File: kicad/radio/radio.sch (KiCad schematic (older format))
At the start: 52 parts, among them J1 SDA, J2 SCL, J3 +5v, J4 +5v, J5 GND1/+12v, J5 GND2, J6 Audio Out, J6 GND2, J7 Antennas, Q1 2N7000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

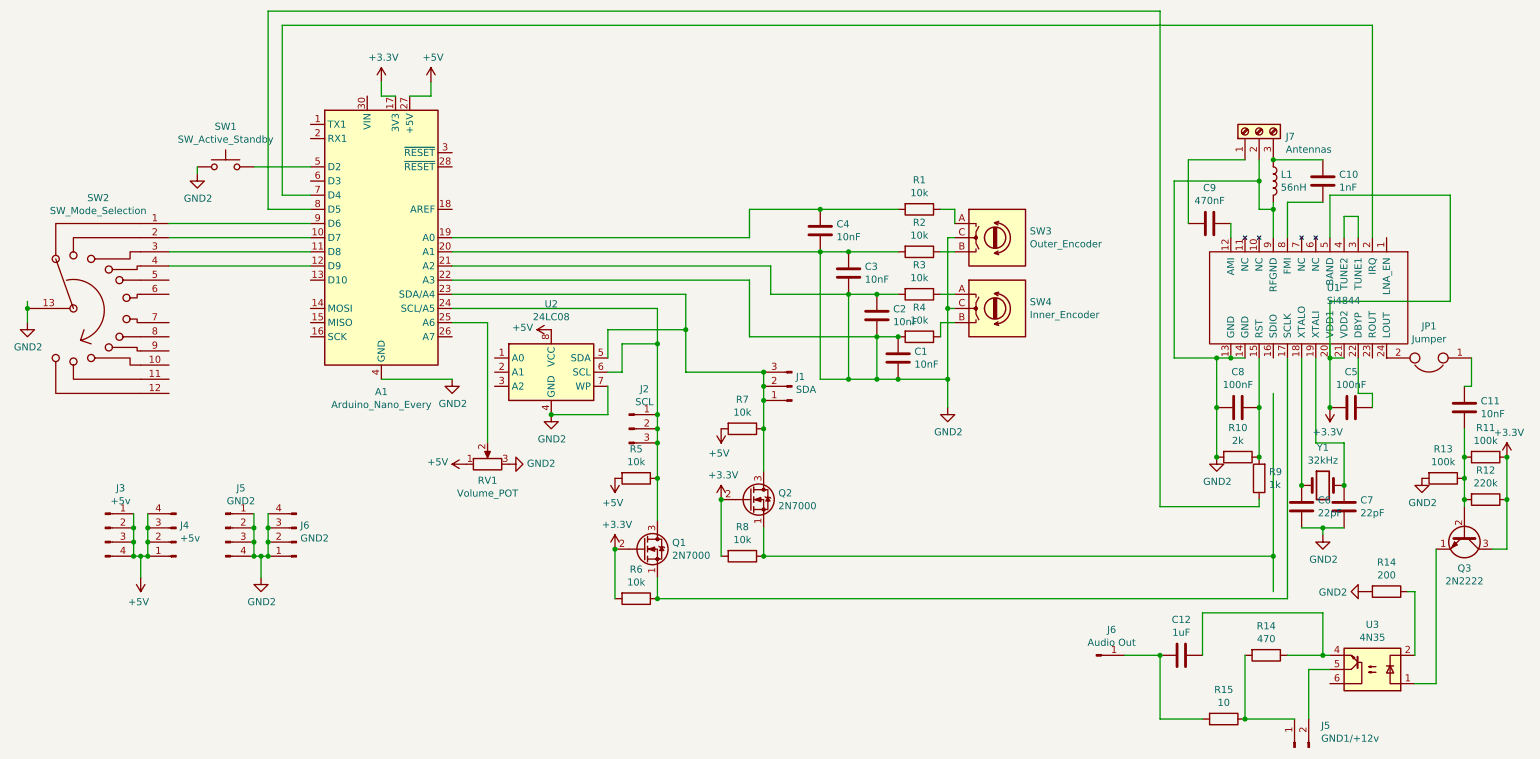
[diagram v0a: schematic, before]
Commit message: improved radio and amplifier schematic
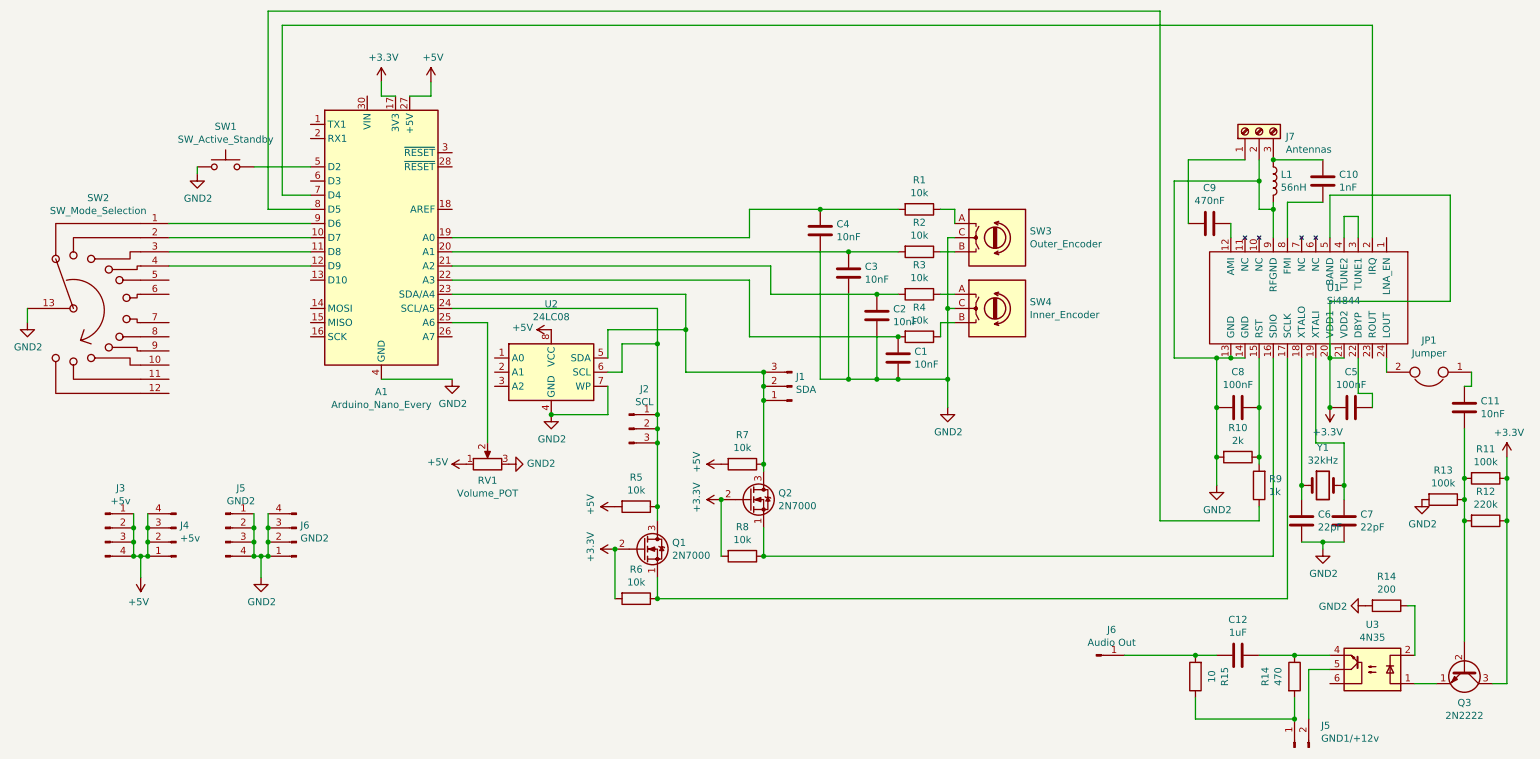
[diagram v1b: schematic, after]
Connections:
- net GND2: no longer A1.20 (A1), A1.21 (A2), A1.22 (A3), C1.2, C2.2, C3.2, R2.2, R3.2, R4.2
- net at U1.16 (SDIO): now also Q2.1 (S), R8.1
- new net: A1.20 (A1), C3.2, R2.2
- new net: A1.21 (A2), C2.2, R3.2
- new net: A1.22 (A3), C1.2, R4.2
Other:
- moved on the sheet: C12, C6, C7, JP1, Q3, R11, R12, R13, R14, R15, R5, R7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

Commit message: Power supply modifications
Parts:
- added C13: 100uF, symbol Device:CP
- added J6: GND2/+5v, symbol Connector:Conn_01x02_Male
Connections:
- net +5V: now also C13.1, J6.2 (Pin_2)
- net GND2: now also C13.2, J6.1 (Pin_1)

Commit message: Only activate squelch after AM transmission is picked up
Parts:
- renumbered J6 to J10, J6 to J8, J5 to J9, R14 to R16
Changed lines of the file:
@@
 Connection ~ 1400 4750
 $Comp
-L Connector:Conn_01x04_Male J5
+L Connector:Conn_01x04_Male J9
 U 1 1 610CF0CD
 P 1950 4750
-F 0 "J5" H 2058 5031 50  0000 C CNN
+F 0 "J9" H 2058 5031 50  0000 C CNN
 F 1 "GND2" H 2058 4940 50  0000 C CNN
 F 2 "" H 1950 4750 50  0001 C CNN
@@
 $EndComp
 $Comp
-L Connector:Conn_01x04_Male J6
+L Connector:Conn_01x04_Male J8
 U 1 1 610CFD7C
 P 2450 4850
-F 0 "J6" H 2422 4732 50  0000 R CNN
+F 0 "J8" H 2422 4732 50  0000 R CNN
 F 1 "GND2" H 2422 4823 50  0000 R CNN
 F 2 "" H 2450 4850 50  0001 C CNN
@@
 	9600 5750 9750 5750
 $Comp
-L Device:R R14
+L Device:R R16
 U 1 1 613D5245
 P 9500 5800
-F 0 "R14" V 9293 5800 50  0000 C CNN
+F 0 "R16" V 9293 5800 50  0000 C CNN
 F 1 "470" V 9384 5800 50  0000 C CNN
 F 2 "" V 9430 5800 50  0001 C CNN
@@
 $EndComp
 $Comp
-L power:GND2 #PWR?
+L power:GND2 #PWR0101
 U 1 1 61086458
 P 3650 1700
-F 0 "#PWR?" H 3650 1450 50  0001 C CNN
+F 0 "#PWR0101" H 3650 1450 50  0001 C CNN
 F 1 "GND2" H 3655 1527 50  0000 C CNN
 F 2 "" H 3650 1700 50  0001 C CNN
@@
 $EndComp
 $Comp
-L Connector:Conn_01x02_Male J6
+L Connector:Conn_01x02_Male J10
 U 1 1 61086AD9
 P 3900 1900
-F 0 "J6" V 4054 1712 50  0000 R CNN
+F 0 "J10" V 4054 1712 50  0000 R CNN
 F 1 "GND2/+5v" V 3963 1712 50  0000 R CNN
 F 2 "" H 3900 1900 50  0001 C CNN
